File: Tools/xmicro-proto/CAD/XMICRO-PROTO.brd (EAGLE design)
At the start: 203.2 x 101.6 mm, 1 part

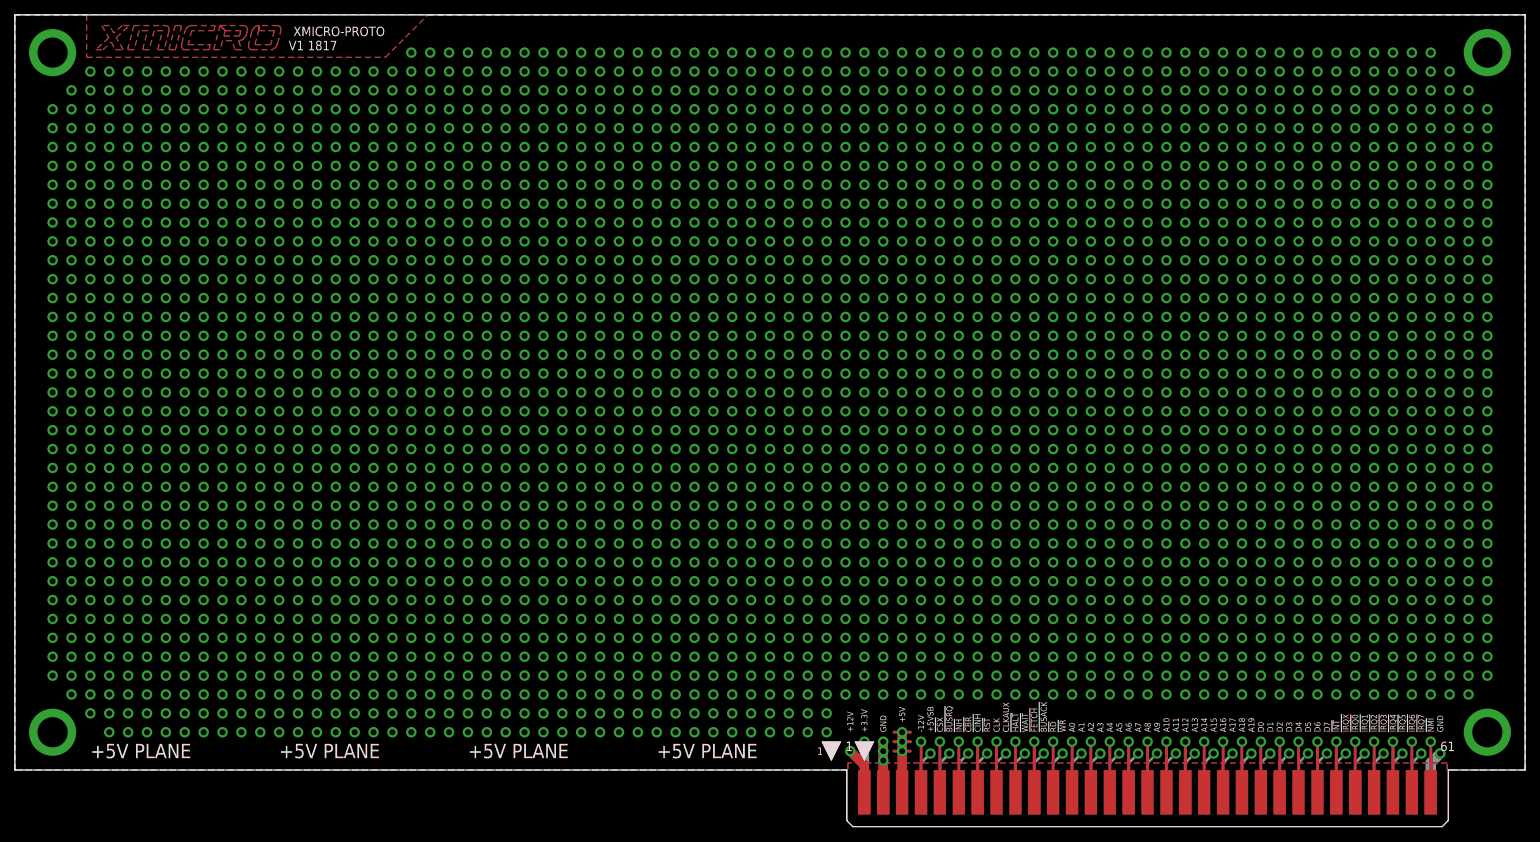
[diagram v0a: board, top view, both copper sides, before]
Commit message: Fixed tools with new IOSEL signal
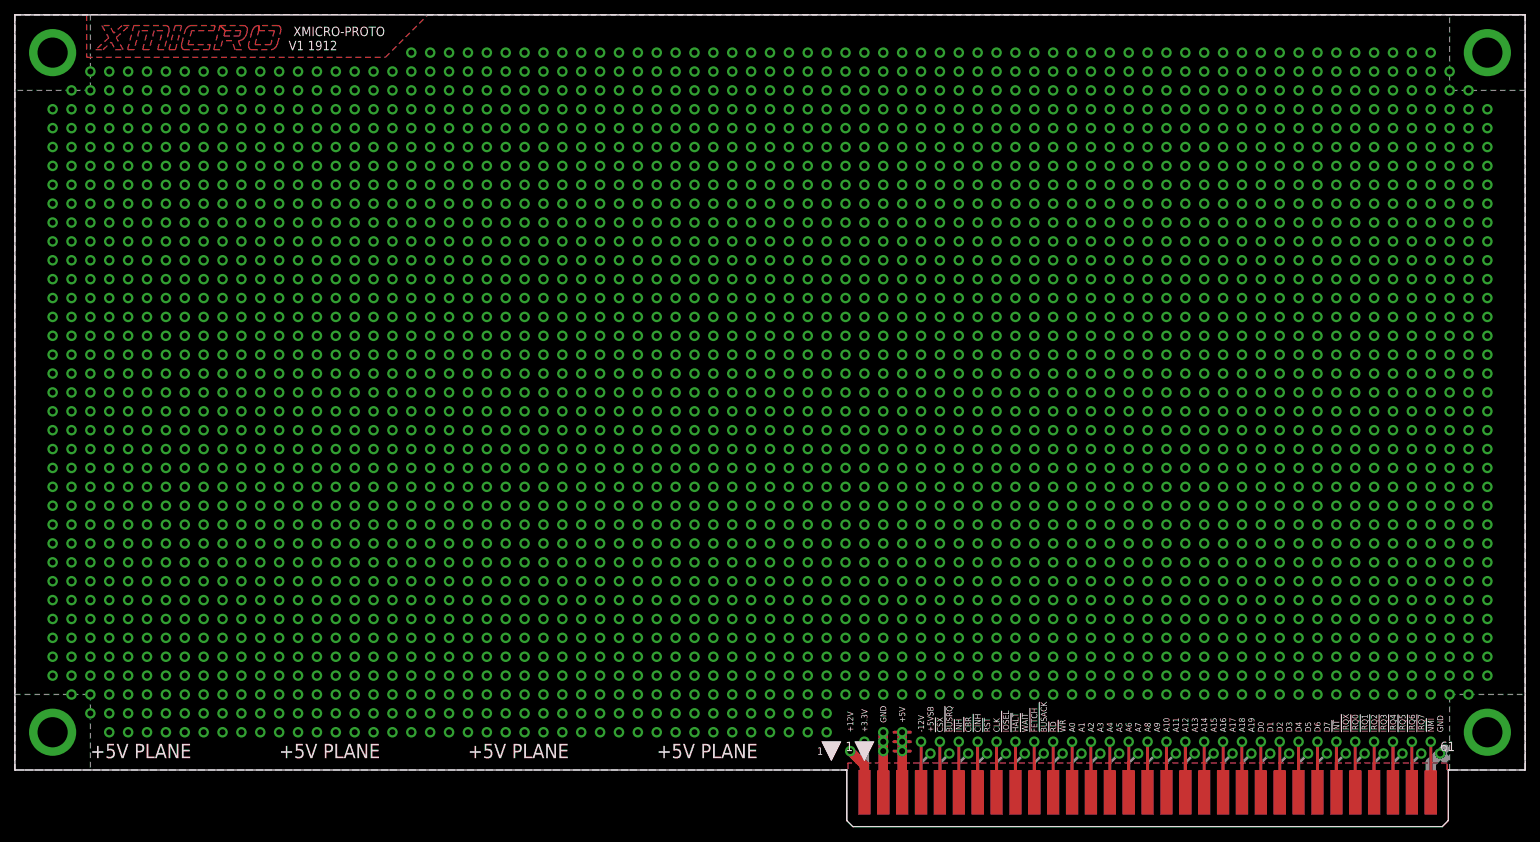
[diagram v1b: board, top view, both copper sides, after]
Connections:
- net CLKAUX renamed !IOSEL
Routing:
- net GND: track 19.4 -> 23.7 mm
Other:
- board text added: "!IOSEL"
- board text added: "V1 1912"
- board text removed: "CLKAUX"
- board text removed: "V1 1817"
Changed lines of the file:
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@@
 <setting verticaltext="up"/>
 </settings>
-<grid distance="0.1" unitdist="inch" unit="inch" style="dots" multiple="1" display="no" altdistance="0.00625" altunitdist="inch" altunit="inch"/>
+<grid distance="0.05" unitdist="inch" unit="inch" style="dots" multiple="1" display="no" altdistance="0.0125" altunitdist="inch" altunit="inch"/>
 <layers>
 <layer number="1" name="Top" color="4" fill="1" visible="yes" active="yes"/>
@@
 <layer number="39" name="tKeepout" color="4" fill="11" visible="no" active="yes"/>
 <layer number="40" name="bKeepout" color="1" fill="11" visible="no" active="yes"/>
-<layer number="41" name="tRestrict" color="4" fill="10" visible="no" active="yes"/>
-<layer number="42" name="bRestrict" color="1" fill="10" visible="no" active="yes"/>
+<layer number="41" name="tRestrict" color="4" fill="10" visible="yes" active="yes"/>
+<layer number="42" name="bRestrict" color="1" fill="10" visible="yes" active="yes"/>
 <layer number="43" name="vRestrict" color="2" fill="10" visible="no" active="yes"/>
 <layer number="44" name="Drills" color="7" fill="1" visible="no" active="yes"/>
@@
 <text x="60.96" y="1.5875" size="1.9304" layer="21" font="vector" ratio="15">+5V PLANE</text>
 <text x="37.465" y="98.7425" size="1.27" layer="21" font="vector" ratio="15">XMICRO-PROTO</text>
-<text x="36.83" y="96.8375" size="1.27" layer="21" font="vector" ratio="15">V1 1817</text>
+<text x="36.83" y="96.8375" size="1.27" layer="21" font="vector" ratio="15">V1 1912</text>
 <text x="112.395" y="5.08" size="0.8128" layer="25" font="vector" ratio="12" rot="R90" align="center-left">+12V</text>
 <text x="121.92" y="5.08" size="0.8128" layer="25" font="vector" ratio="12" rot="R90" align="center-left">-12V</text>
 <text x="123.19" y="5.08" size="0.8128" layer="25" font="vector" ratio="12" rot="R90" align="center-left">+5VSB</text>
 <text x="119.38" y="6.35" size="0.8128" layer="25" font="vector" ratio="12" rot="R90" align="center-left">+5V</text>
-<text x="116.84" y="5.08" size="0.8128" layer="25" font="vector" ratio="12" rot="R90" align="center-left">GND</text>
+<text x="116.84" y="6.35" size="0.8128" layer="25" font="vector" ratio="12" rot="R90" align="center-left">GND</text>
 <text x="114.3" y="5.08" size="0.8128" layer="25" font="vector" ratio="12" rot="R90" align="center-left">+3.3V</text>
 <text x="124.46" y="5.08" size="0.8128" layer="25" font="vector" ratio="12" rot="R90" align="center-left">!CSX</text>
@@
 <text x="130.81" y="5.08" size="0.8128" layer="25" font="vector" ratio="12" rot="R90" align="center-left">!RST</text>
 <text x="132.08" y="5.08" size="0.8128" layer="25" font="vector" ratio="12" rot="R90" align="center-left">CLK</text>
-<text x="133.35" y="5.08" size="0.8128" layer="25" font="vector" ratio="12" rot="R90" align="center-left">CLKAUX</text>
+<text x="133.35" y="5.08" size="0.8128" layer="25" font="vector" ratio="12" rot="R90" align="center-left">!IOSEL</text>
 <text x="134.62" y="5.08" size="0.8128" layer="25" font="vector" ratio="12" rot="R90" align="center-left">!HALT</text>
 <text x="135.89" y="5.08" size="0.8128" layer="25" font="vector" ratio="12" rot="R90" align="center-left">!WAIT</text>
@@
 <text x="86.36" y="1.5875" size="1.9304" layer="21" font="vector" ratio="15">+5V PLANE</text>
 <text x="86.36" y="1.5875" size="1.9304" layer="22" font="vector" ratio="15" rot="MR0" align="bottom-right">GND PLANE</text>
-<circle x="5.08" y="5.08" radius="4.016090625" width="0.127" layer="41"/>
-<circle x="5.08" y="96.52" radius="4.016090625" width="0.127" layer="41"/>
-<circle x="198.12" y="96.52" radius="4.016090625" width="0.127" layer="41"/>
-<circle x="198.12" y="5.08" radius="4.016090625" width="0.127" layer="41"/>
-<wire x1="118.4275" y1="0.79375" x2="118.4275" y2="5.08" width="0.254" layer="41"/>
-<wire x1="120.3325" y1="5.08" x2="120.3325" y2="0.79375" width="0.254" layer="41"/>
+<circle x="5.08" y="5.08" radius="5.08" width="0.127" layer="41"/>
+<circle x="5.08" y="96.52" radius="5.08" width="0.127" layer="41"/>
+<circle x="198.12" y="96.52" radius="5.08" width="0.127" layer="41"/>
+<circle x="198.12" y="5.08" radius="5.08" width="0.127" layer="41"/>
+<wire x1="118.4275" y1="1.905" x2="118.4275" y2="5.08" width="0.254" layer="41"/>
+<wire x1="120.3325" y1="5.08" x2="120.3325" y2="1.905" width="0.254" layer="41"/>
 <polygon width="0.4064" layer="42">
 <vertex x="191.135" y="3.175"/>
@@
 <text x="123.19" y="5.08" size="0.8128" layer="26" font="vector" ratio="12" rot="SMR270" align="center-right">+5VSB</text>
 <text x="119.38" y="6.35" size="0.8128" layer="26" font="vector" ratio="12" rot="SMR270" align="center-right">+5V</text>
-<text x="116.84" y="5.08" size="0.8128" layer="26" font="vector" ratio="12" rot="SMR270" align="center-right">GND</text>
+<text x="116.84" y="6.35" size="0.8128" layer="26" font="vector" ratio="12" rot="SMR270" align="center-right">GND</text>
 <text x="114.3" y="5.08" size="0.8128" layer="26" font="vector" ratio="12" rot="SMR270" align="center-right">+3.3V</text>
 <text x="124.46" y="5.08" size="0.8128" layer="26" font="vector" ratio="12" rot="SMR270" align="center-right">!CSX</text>
@@
 <text x="130.81" y="5.08" size="0.8128" layer="26" font="vector" ratio="12" rot="SMR270" align="center-right">!RST</text>
 <text x="132.08" y="5.08" size="0.8128" layer="26" font="vector" ratio="12" rot="SMR270" align="center-right">CLK</text>
-<text x="133.35" y="5.08" size="0.8128" layer="26" font="vector" ratio="12" rot="SMR270" align="center-right">CLKAUX</text>
+<text x="133.35" y="5.08" size="0.8128" layer="26" font="vector" ratio="12" rot="SMR270" align="center-right">!IOSEL</text>
 <text x="134.62" y="5.08" size="0.8128" layer="26" font="vector" ratio="12" rot="SMR270" align="center-right">!HALT</text>
 <text x="135.89" y="5.08" size="0.8128" layer="26" font="vector" ratio="12" rot="SMR270" align="center-right">!WAIT</text>
@@
 <wire x1="190.5" y1="0.9525" x2="191.77" y2="2.2225" width="1.4224" layer="16"/>
 <via x="191.77" y="2.2225" extent="1-16" drill="0.8" diameter="1.4224" alwaysstop="yes"/>
-<wire x1="116.84" y1="-3.0099" x2="116.84" y2="1.27" width="1.27" layer="1"/>
-<wire x1="116.84" y1="1.27" x2="116.84" y2="2.54" width="1.27" layer="1"/>
+<wire x1="116.84" y1="-3.0099" x2="116.84" y2="2.54" width="1.27" layer="1"/>
 <wire x1="116.84" y1="2.54" x2="116.84" y2="3.81" width="1.27" layer="1"/>
-<wire x1="116.84" y1="-3.0099" x2="116.84" y2="1.27" width="1.27" layer="16"/>
-<wire x1="116.84" y1="1.27" x2="116.84" y2="2.54" width="1.27" layer="16"/>
+<wire x1="116.84" y1="3.81" x2="116.84" y2="5.08" width="1.27" layer="1"/>
+<wire x1="116.84" y1="-3.0099" x2="116.84" y2="2.54" width="1.27" layer="16"/>
 <wire x1="116.84" y1="2.54" x2="116.84" y2="3.81" width="1.27" layer="16"/>
+<wire x1="116.84" y1="3.81" x2="116.84" y2="5.08" width="1.27" layer="16"/>
+<via x="116.84" y="5.08" extent="1-16" drill="0.8" diameter="1.4224" alwaysstop="yes"/>
 <via x="116.84" y="3.81" extent="1-16" drill="0.8" diameter="1.4224" alwaysstop="yes"/>
 <via x="116.84" y="2.54" extent="1-16" drill="0.8" diameter="1.4224" alwaysstop="yes"/>
-<via x="116.84" y="1.27" extent="1-16" drill="0.8" diameter="1.4224" alwaysstop="yes"/>
 <via x="198.12" y="5.08" extent="1-16" drill="4.064" diameter="6.35" alwaysstop="yes"/>
 <via x="198.12" y="96.52" extent="1-16" drill="4.064" diameter="6.35" alwaysstop="yes"/>
 <via x="5.08" y="5.08" extent="1-16" drill="4.064" diameter="6.35" alwaysstop="yes"/>
 <via x="5.08" y="96.52" extent="1-16" drill="4.064" diameter="6.35" alwaysstop="yes"/>
+<wire x1="191.77" y1="2.2225" x2="192.405" y2="1.5875" width="1.27" layer="16"/>
+<wire x1="191.77" y1="2.2225" x2="192.405" y2="2.8575" width="1.27" layer="16"/>
+<polygon width="0.254" layer="16" thermals="no">
+<vertex x="0" y="101.6"/>
+<vertex x="10.16" y="101.6"/>
+<vertex x="10.16" y="91.44"/>
+<vertex x="0" y="91.44"/>
+</polygon>
+<polygon width="0.254" layer="16" thermals="no">
+<vertex x="0" y="10.16"/>
+<vertex x="10.16" y="10.16"/>
+<vertex x="10.16" y="0"/>
+<vertex x="0" y="0"/>
+</polygon>
+<polygon width="0.254" layer="16" thermals="no">
+<vertex x="193.04" y="10.16"/>
+<vertex x="203.2" y="10.16"/>
+<vertex x="203.2" y="0"/>
+<vertex x="193.04" y="0"/>
+</polygon>
+<polygon width="0.254" layer="16" thermals="no">
+<vertex x="193.04" y="101.6"/>
+<vertex x="203.2" y="101.6"/>
+<vertex x="203.2" y="91.44"/>
+<vertex x="193.04" y="91.44"/>
+</polygon>
 </signal>
 <signal name="S$1">
@@
 <via x="132.08" y="3.81" extent="1-16" drill="0.8" diameter="1.4224" alwaysstop="yes"/>
 </signal>
-<signal name="CLKAUX">
-<contactref element="PC0" pad="16"/>
-<wire x1="132.08" y1="-3.0099" x2="132.08" y2="0.9525" width="0.4064" layer="16"/>
-<wire x1="132.08" y1="0.9525" x2="133.35" y2="2.2225" width="0.4064" layer="16"/>
-<via x="133.35" y="2.2225" extent="1-16" drill="0.8" diameter="1.4224" alwaysstop="yes"/>
-</signal>
 <signal name="N$1">
 <via x="53.34" y="96.52" extent="1-16" drill="0.8" diameter="1.4224" alwaysstop="yes"/>
@@
 <via x="109.22" y="5.08" extent="1-16" drill="0.8" diameter="1.4224" alwaysstop="yes"/>
 </signal>
+<signal name="!IOSEL">
+<contactref element="PC0" pad="16"/>
+<wire x1="132.08" y1="-3.0099" x2="132.08" y2="0.9525" width="0.4064" layer="16"/>
+<wire x1="132.08" y1="0.9525" x2="133.35" y2="2.2225" width="0.4064" layer="16"/>
+<via x="133.35" y="2.2225" extent="1-16" drill="0.8" diameter="1.4224" alwaysstop="yes"/>
+</signal>
 </signals>
-<errors>
-</errors>
 </board>
 </drawing>
